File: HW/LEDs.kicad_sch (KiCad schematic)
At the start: 12 parts

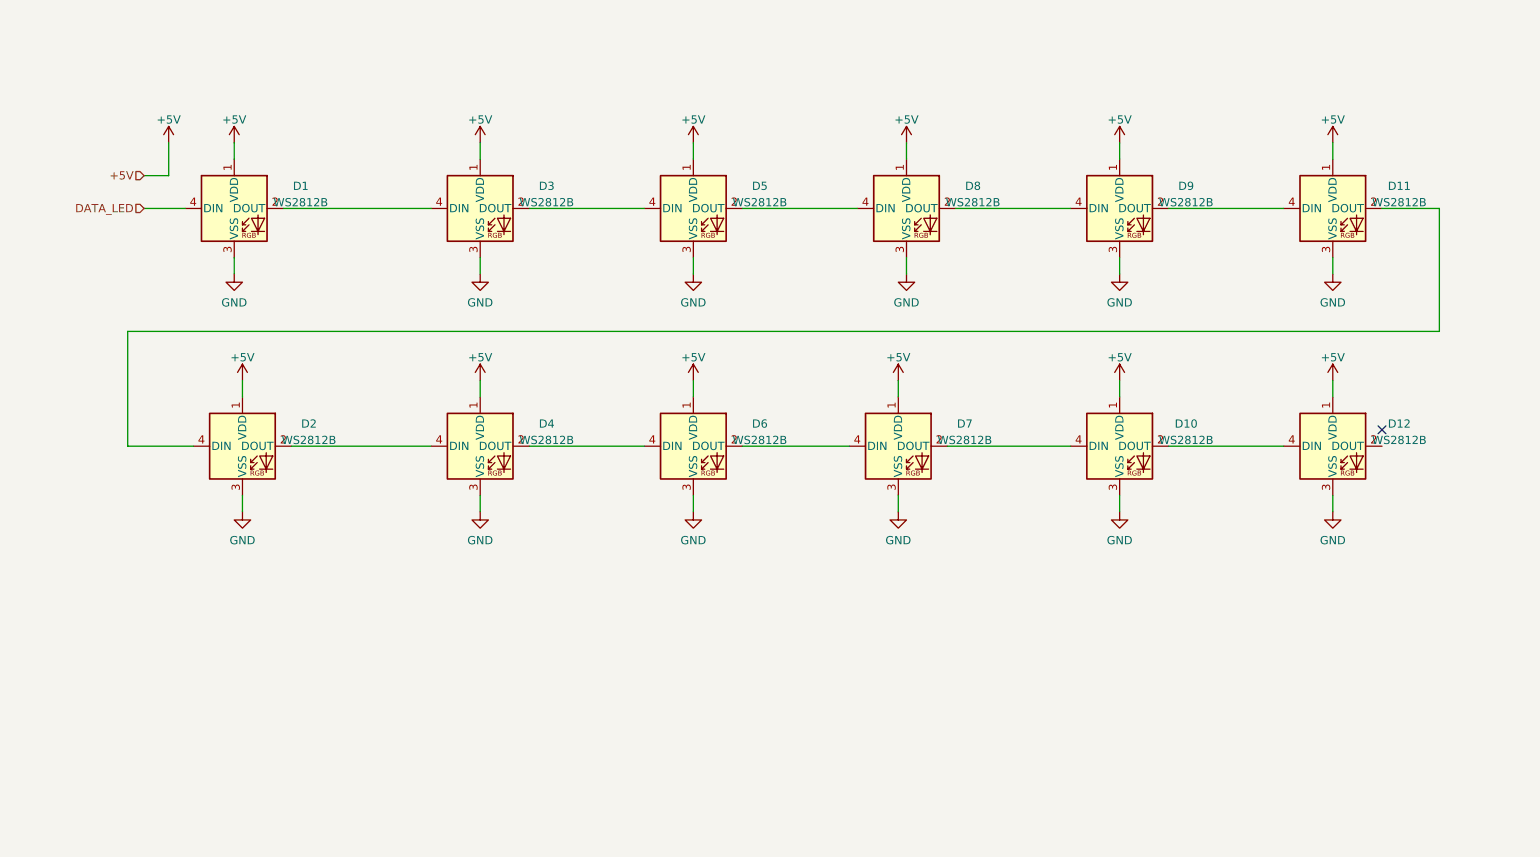
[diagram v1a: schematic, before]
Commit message: update symbol ESP32-C3, add capacitors to WS2812C, add transils to USB
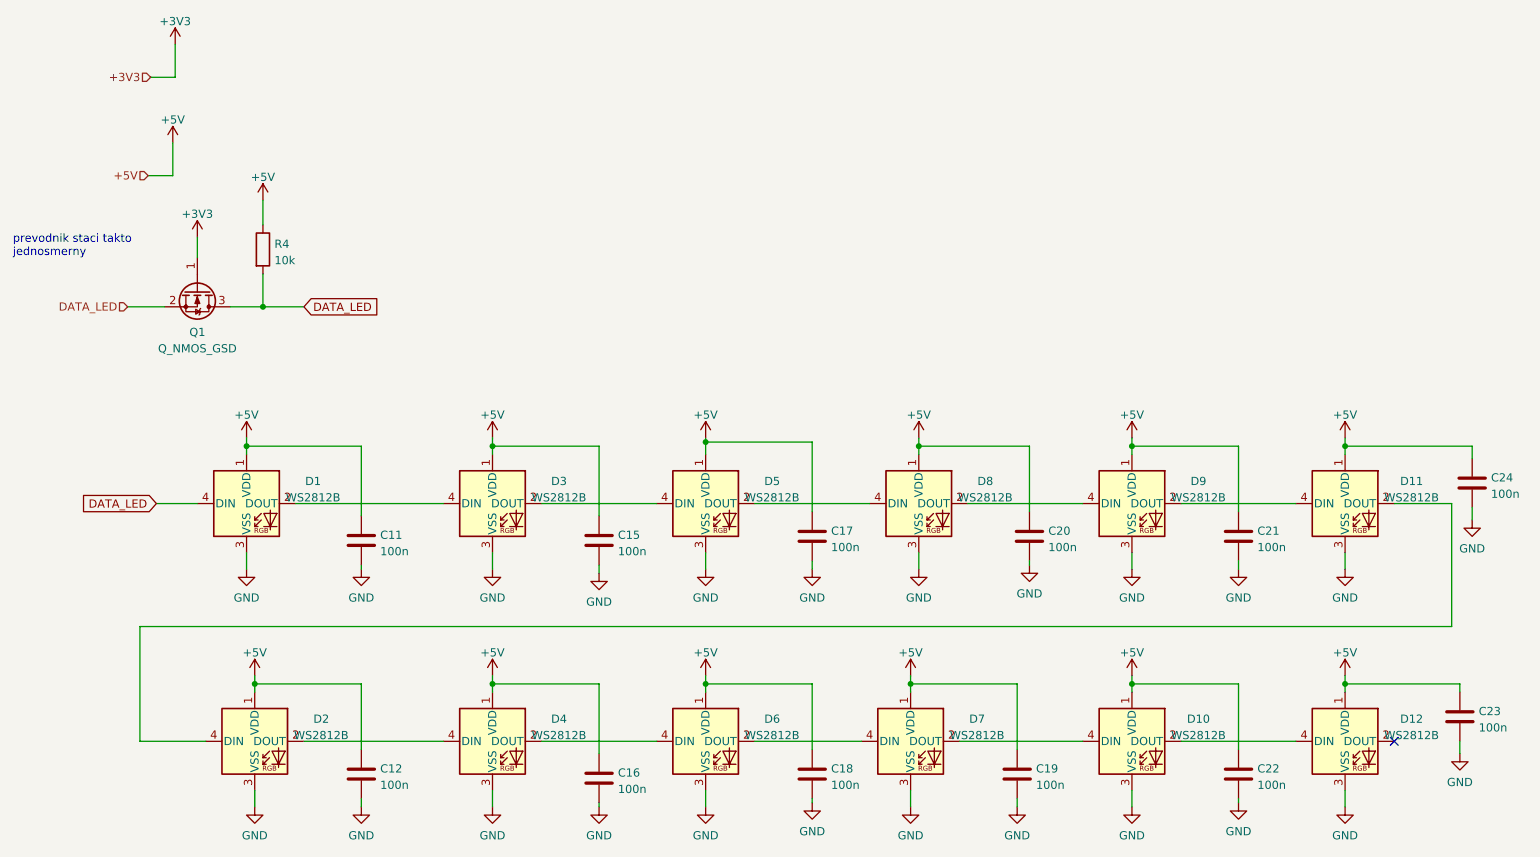
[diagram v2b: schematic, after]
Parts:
- added C11, C12, C15, C16, C17, C18, C19, C20, C21, C22, C23, C24: 100n, Capacitor_SMD:C_0603_1608Metric, symbol Device:C
- added Q1: Q_NMOS_GSD, Package_TO_SOT_SMD:SOT-23, symbol Device:Q_NMOS_GSD
- added R4: 10k, Resistor_SMD:R_0603_1608Metric, symbol Device:R
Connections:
- net +5V: now also C11.1, C12.1, C15.1, C16.1, C17.1, C18.1, C19.1, C20.1, C21.1, C22.1, C23.1, C24.1, R4.1
- net DATA_LED: now also Q1.2 (S), Q1.3 (D), R4.2
- net GND: now also C11.2, C12.2, C15.2, C16.2, C17.2, C18.2, C19.2, C20.2, C21.2, C22.2, C23.2, C24.2
- new net +3V3: Q1.1 (G)
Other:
- note added: "prevodnik staci takto jednosmerny"
- moved on the sheet: D1, D10, D11, D12, D2, D3, D4, D5, D6, D7, D8, D9

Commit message: routing PCB - LEDs
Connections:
- net at D1.2 (DOUT): now also D2.4 (DIN); no longer D3.4 (DIN)
- net at D11.2 (DOUT): now also D12.4 (DIN); no longer D2.4 (DIN)
- net at D11.4 (DIN): now also D10.2 (DOUT); no longer D9.2 (DOUT)
- net at D4.2 (DOUT): now also D5.4 (DIN); no longer D6.4 (DIN)
- net at D4.4 (DIN): now also D3.2 (DOUT); no longer D2.2 (DOUT)
- net at D10.4 (DIN): now also D9.2 (DOUT); no longer D7.2 (DOUT)
- net at D5.2 (DOUT): now also D6.4 (DIN); no longer D8.4 (DIN)
- new net: D2.2 (DOUT), D3.4 (DIN)
- new net: D7.2 (DOUT), D8.4 (DIN)
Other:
- moved on the sheet: D10, D11, D2, D3, D4, D5, D6, D7, D8, D9

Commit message: add fill of description field
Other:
- title: (none) -> WS2812C
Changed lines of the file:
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@@
 (kicad_sch (version 20211123) (generator eeschema)
   (paper "A4")
+  (title_block
+    (title "WS2812C")
+    (rev "1")
+  )
   (junction (at 104.775 92.71) (diameter 0) (color 0 0 0 0)
   )

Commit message: repair mistakes in schematic, add switched supply voltage to LoRa, LEDs and converter for capacitive buttons
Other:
- note removed: "prevodnik staci takto jednosmerny"
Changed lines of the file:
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@@
     (stroke (width 0) (type default) (color 0 0 0 0))
-  )
-  (text "prevodnik staci takto\njednosmerny\n" (at 30.48 63.5 0)
-    (effects (font (size 1.27 1.27)) (justify left bottom))
   )
   (global_label "DATA_LED" (shape input) (at 52.705 101.6 180) (fields_autoplaced)

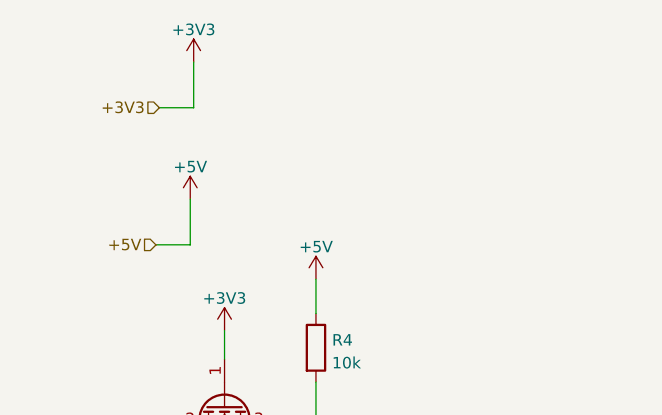
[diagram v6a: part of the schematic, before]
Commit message: repair ERC errors
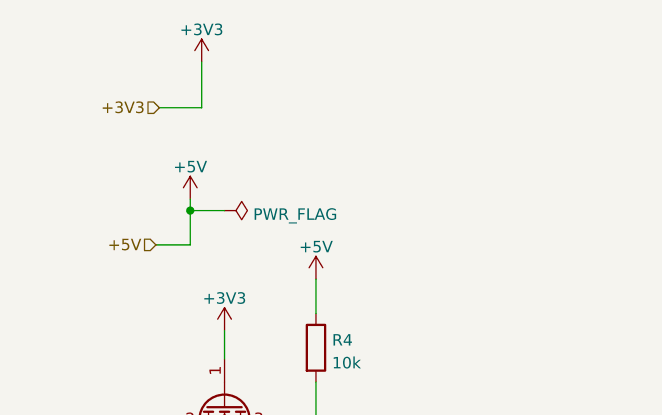
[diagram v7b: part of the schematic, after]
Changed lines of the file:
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@@
   (junction (at 69.215 71.12) (diameter 0) (color 0 0 0 0)
+  )
+  (junction (at 55.245 46.99) (diameter 0) (color 0 0 0 0)
   )
   (junction (at 169.545 129.54) (diameter 0) (color 0 0 0 0)
@@
     (stroke (width 0) (type default) (color 0 0 0 0))
   )
-  (wire (pts (xy 55.245 45.72) (xy 55.245 50.8))
+  (wire (pts (xy 55.245 45.72) (xy 55.245 46.99))
     (stroke (width 0) (type default) (color 0 0 0 0))
   )
@@
     (stroke (width 0) (type default) (color 0 0 0 0))
   )
+  (wire (pts (xy 55.245 46.99) (xy 55.245 50.8))
+    (stroke (width 0) (type default) (color 0 0 0 0))
+  )
   (wire (pts (xy 121.285 92.71) (xy 104.775 92.71))
     (stroke (width 0) (type default) (color 0 0 0 0))
@@
     (stroke (width 0) (type default) (color 0 0 0 0))
   )
+  (wire (pts (xy 55.245 46.99) (xy 59.055 46.99))
+    (stroke (width 0) (type default) (color 0 0 0 0))
+  )
   (wire (pts (xy 236.855 146.05) (xy 236.855 148.59))
     (stroke (width 0) (type default) (color 0 0 0 0))
   )
-  (wire (pts (xy 55.626 30.48) (xy 55.626 35.56))
-    (stroke (width 0) (type default) (color 0 0 0 0))
-  )
   (wire (pts (xy 170.815 91.44) (xy 170.815 92.71))
     (stroke (width 0) (type default) (color 0 0 0 0))
@@
     (stroke (width 0) (type default) (color 0 0 0 0))
   )
-  (wire (pts (xy 55.626 35.56) (xy 51.816 35.56))
+  (wire (pts (xy 51.816 35.56) (xy 56.515 35.56))
     (stroke (width 0) (type default) (color 0 0 0 0))
   )
@@
   )
   (wire (pts (xy 104.775 129.54) (xy 104.775 130.81))
+    (stroke (width 0) (type default) (color 0 0 0 0))
+  )
+  (wire (pts (xy 56.515 30.48) (xy 56.515 35.56))
     (stroke (width 0) (type default) (color 0 0 0 0))
   )
@@
     (pin "1")
   )
+  (symbol (lib_id "power:PWR_FLAG") (at 59.055 46.99 270) (unit 1)
+    (in_bom yes) (on_board yes) (fields_autoplaced)
+    (property "Reference" "#FLG0105" (id 0) (at 60.96 46.99 0)
+      (effects (font (size 1.27 1.27)) hide)
+    )
+    (property "Value" "PWR_FLAG" (id 1) (at 62.23 47.4238 90)
+      (effects (font (size 1.27 1.27)) (justify left))
+    )
+    (property "Footprint" "" (id 2) (at 59.055 46.99 0)
+      (effects (font (size 1.27 1.27)) hide)
+    )
+    (property "Datasheet" "~" (id 3) (at 59.055 46.99 0)
+      (effects (font (size 1.27 1.27)) hide)
+    )
+    (pin "1")
+  )
   (symbol (lib_id "power:GND") (at 104.775 111.76 0) (unit 1)
     (in_bom yes) (on_board yes) (fields_autoplaced)
@@
     (pin "1")
   )
-  (symbol (lib_id "power:+3V3") (at 55.626 30.48 0) (unit 1)
-    (in_bom yes) (on_board yes) (fields_autoplaced)
-    (property "Reference" "#PWR0181" (id 0) (at 55.626 34.29 0)
-      (effects (font (size 1.27 1.27)) hide)
-    )
-    (property "Value" "+3V3" (id 1) (at 55.626 26.9042 0))
-    (property "Footprint" "" (id 2) (at 55.626 30.48 0)
-      (effects (font (size 1.27 1.27)) hide)
-    )
-    (property "Datasheet" "" (id 3) (at 55.626 30.48 0)
-      (effects (font (size 1.27 1.27)) hide)
-    )
+  (symbol (lib_id "power:+3V3") (at 56.515 30.48 0) (unit 1)
+    (in_bom yes) (on_board yes) (fields_autoplaced)
+    (property "Reference" "#PWR0181" (id 0) (at 56.515 34.29 0)
+      (effects (font (size 1.27 1.27)) hide)
+    )
+    (property "Value" "+3V3" (id 1) (at 56.515 26.9042 0))
+    (property "Footprint" "" (id 2) (at 56.515 30.48 0)
+      (effects (font (size 1.27 1.27)) hide)
+    )
+    (property "Datasheet" "" (id 3) (at 56.515 30.48 0)
+      (effects (font (size 1.27 1.27)) hide)
+    )

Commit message: add some codes for assembly byJLCPCB
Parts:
- C11, C12, C15, C16, C17, C18, C19, C20, C21, C22, C23, C24: LCSC (none) -> C14663
- D1, D10, D11, D12, D2, D3, D4, D5, D6, D7, D8, D9: LCSC (none) -> C2761796
- R4: LCSC (none) -> C25804
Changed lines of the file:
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@@
+      (effects (font (size 1.27 1.27)) hide)
+    )
+    (property "LCSC" "C14663" (id 4) (at 84.455 107.315 0)
       (effects (font (size 1.27 1.27)) hide)
     )
@@
       (effects (font (size 1.27 1.27)) hide)
     )
+    (property "LCSC" "C14663" (id 4) (at 256.54 98.425 0)
+      (effects (font (size 1.27 1.27)) hide)
+    )
     (pin "1")
     (pin "2")
@@
     )
     (property "Datasheet" "~" (id 3) (at 220.345 143.51 0)
+      (effects (font (size 1.27 1.27)) hide)
+    )
+    (property "LCSC" "C14663" (id 4) (at 220.345 143.51 0)
       (effects (font (size 1.27 1.27)) hide)
     )
@@
       (effects (font (size 1.27 1.27)) hide)
     )
+    (property "LCSC" "C14663" (id 4) (at 187.96 106.68 0)
+      (effects (font (size 1.27 1.27)) hide)
+    )
     (pin "1")
     (pin "2")
@@
     )
     (property "Datasheet" "~" (id 3) (at 186.055 143.51 0)
+      (effects (font (size 1.27 1.27)) hide)
+    )
+    (property "LCSC" "C14663" (id 4) (at 186.055 143.51 0)
       (effects (font (size 1.27 1.27)) hide)
     )
@@
       (effects (font (size 1.27 1.27)) (justify left top) hide)
     )
+    (property "LCSC" "C2761796" (id 4) (at 66.675 101.6 0)
+      (effects (font (size 1.27 1.27)) hide)
+    )
     (pin "1")
     (pin "2")
@@
       (effects (font (size 1.27 1.27)) (justify left top) hide)
     )
+    (property "LCSC" "C2761796" (id 4) (at 203.835 138.43 0)
+      (effects (font (size 1.27 1.27)) hide)
+    )
     (pin "1")
     (pin "2")
@@
       (effects (font (size 1.27 1.27)) (justify left top) hide)
     )
+    (property "LCSC" "C2761796" (id 4) (at 170.815 101.6 0)
+      (effects (font (size 1.27 1.27)) hide)
+    )
     (pin "1")
     (pin "2")
@@
       (effects (font (size 1.27 1.27)) (justify left top) hide)
     )
+    (property "LCSC" "C2761796" (id 4) (at 169.545 138.43 0)
+      (effects (font (size 1.27 1.27)) hide)
+    )
     (pin "1")
     (pin "2")
@@
     )
     (property "Datasheet" "~" (id 3) (at 154.305 106.68 0)
+      (effects (font (size 1.27 1.27)) hide)
+    )
+    (property "LCSC" "C14663" (id 4) (at 154.305 106.68 0)
       (effects (font (size 1.27 1.27)) hide)
     )
@@
       (effects (font (size 1.27 1.27)) (justify left top) hide)
     )
+    (property "LCSC" "C2761796" (id 4) (at 203.835 101.6 0)
+      (effects (font (size 1.27 1.27)) hide)
+    )
     (pin "1")
     (pin "2")
@@
       (effects (font (size 1.27 1.27)) (justify left top) hide)
     )
+    (property "LCSC" "C2761796" (id 4) (at 137.795 101.6 0)
+      (effects (font (size 1.27 1.27)) hide)
+    )
     (pin "1")
     (pin "2")
@@
     )
     (property "Datasheet" "~" (id 3) (at 121.285 144.145 0)
+      (effects (font (size 1.27 1.27)) hide)
+    )
+    (property "LCSC" "C14663" (id 4) (at 121.285 144.145 0)
       (effects (font (size 1.27 1.27)) hide)
     )
@@
       (effects (font (size 1.27 1.27)) (justify left top) hide)
     )
+    (property "LCSC" "C2761796" (id 4) (at 104.775 138.43 0)
+      (effects (font (size 1.27 1.27)) hide)
+    )
     (pin "1")
     (pin "2")
@@
       (effects (font (size 1.27 1.27)) hide)
     )
+    (property "LCSC" "C14663" (id 4) (at 154.305 143.51 0)
+      (effects (font (size 1.27 1.27)) hide)
+    )
     (pin "1")
     (pin "2")
@@
       (effects (font (size 1.27 1.27)) hide)
     )
+    (property "LCSC" "C14663" (id 4) (at 84.455 143.51 0)
+      (effects (font (size 1.27 1.27)) hide)
+    )
     (pin "1")
     (pin "2")
@@
     )
     (property "Datasheet" "~" (id 3) (at 121.285 107.315 0)
+      (effects (font (size 1.27 1.27)) hide)
+    )
+    (property "LCSC" "C14663" (id 4) (at 121.285 107.315 0)
       (effects (font (size 1.27 1.27)) hide)
     )
@@
     )
     (property "Datasheet" "~" (id 3) (at 69.215 62.23 0)
+      (effects (font (size 1.27 1.27)) hide)
+    )
+    (property "LCSC" "C25804" (id 4) (at 69.215 62.23 0)
       (effects (font (size 1.27 1.27)) hide)
     )
@@
       (effects (font (size 1.27 1.27)) (justify left top) hide)
     )
+    (property "LCSC" "C2761796" (id 4) (at 236.855 138.43 0)
+      (effects (font (size 1.27 1.27)) hide)
+    )
     (pin "1")
     (pin "2")
@@
       (effects (font (size 1.27 1.27)) (justify left top) hide)
     )
+    (property "LCSC" "C2761796" (id 4) (at 236.855 101.6 0)
+      (effects (font (size 1.27 1.27)) hide)
+    )
     (pin "1")
     (pin "2")
@@
     )
     (property "Datasheet" "~" (id 3) (at 254.635 134.62 0)
+      (effects (font (size 1.27 1.27)) hide)
+    )
+    (property "LCSC" "C14663" (id 4) (at 254.635 134.62 0)
       (effects (font (size 1.27 1.27)) hide)
     )
@@
       (effects (font (size 1.27 1.27)) (justify left top) hide)
     )
+    (property "LCSC" "C2761796" (id 4) (at 137.795 138.43 0)
+      (effects (font (size 1.27 1.27)) hide)
+    )
     (pin "1")
     (pin "2")
@@
     )
     (property "Datasheet" "~" (id 3) (at 220.345 106.68 0)
+      (effects (font (size 1.27 1.27)) hide)
+    )
+    (property "LCSC" "C14663" (id 4) (at 220.345 106.68 0)
       (effects (font (size 1.27 1.27)) hide)
     )
@@
       (effects (font (size 1.27 1.27)) (justify left top) hide)
     )
+    (property "LCSC" "C2761796" (id 4) (at 104.775 101.6 0)
+      (effects (font (size 1.27 1.27)) hide)
+    )
     (pin "1")
     (pin "2")
@@
       (effects (font (size 1.27 1.27)) (justify left top) hide)
     )
-    (pin "1")
+    (property "LCSC" "C2761796" (id 4) (at 67.945 138.43 0)
+      (effects (font (size 1.27 1.27)) hide)
+    )
+    (pin "1")
